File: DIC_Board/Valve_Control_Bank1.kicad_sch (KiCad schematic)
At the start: 10 parts, among them U20 DRV8823QDCARQ1

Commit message: Completed Acid Pump sheet
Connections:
- net GND: no longer C204.2
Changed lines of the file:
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@@
-		)
-	)
-	(label "GND"
-		(at 171.45 69.85 270)
-		(effects
-			(font
-				(size 1.27 1.27)
-			)
-			(justify right bottom)
 		)
 	)

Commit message: Wrapping up schematic
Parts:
- removed R200, R201, R202, R203: 3.3R, Resistor_SMD:R_1206_3216Metric, symbol Device:R_Small_US
- added R318, R319, R330, R331: 3.3R, Resistor_SMD:R_0402_1005Metric, symbol Device:R
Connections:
- net GND: now also C204.2, R318.2, R319.2, R330.2, R331.2
- net at U20.47 (BISEN): now also R319.1
- net at U20.21 (DISEN): now also R331.1
- net at U20.26 (CISEN): now also R330.1
- net at U20.4 (AISEN): now also R318.1
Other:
- moved on the sheet: C200, C201, C202, C203, C204, U20

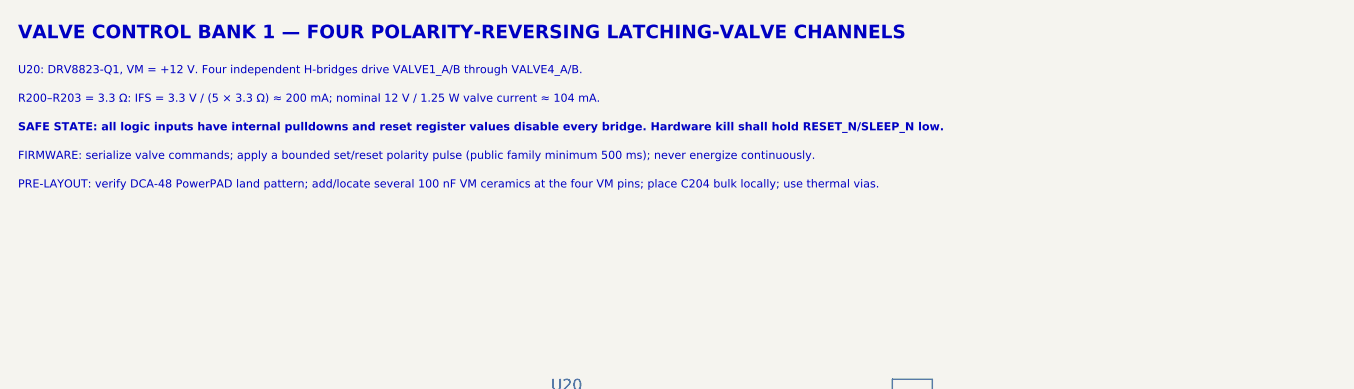
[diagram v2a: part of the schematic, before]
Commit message: Synchronize power, communications, and MCU configuration
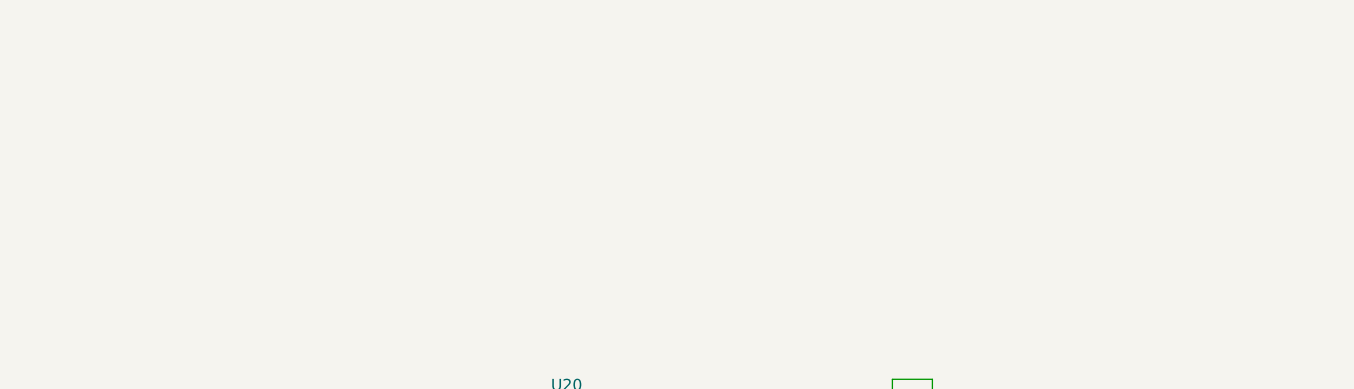
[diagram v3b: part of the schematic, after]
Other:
- note removed: "FIRMWARE: serialize valve commands; apply a bounded set/reset polarity pulse (public family minimum 500 ms); never energize continuously."
- note removed: "PRE-LAYOUT: verify DCA-48 PowerPAD land pattern; add/locate several 100 nF VM ceramics at the four VM pins; place C204 bulk locally; use thermal vias."
- note removed: "R200–R203 = 3.3 Ω: IFS = 3.3 V / (5 × 3.3 Ω) ≈ 200 mA; nominal 12 V / 1.25 W valve current ≈ 104 mA."
- note removed: "SAFE STATE: all logic inputs have internal pulldowns and reset register values disable every bridge. Hardware kill shall hold RESET_N/SLEEP_N low."
- note removed: "U20: DRV8823-Q1, VM = +12 V. Four independent H-bridges drive VALVE1_A/B through VALVE4_A/B."
- note removed: "VALVE CONTROL BANK 1 — FOUR POLARITY-REVERSING LATCHING-VALVE CHANNELS"
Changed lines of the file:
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@@
 		(comment 2 "DRV8823-Q1 serial quad H-bridge")
-	)
-	(text "U20: DRV8823-Q1, VM = +12 V. Four independent H-bridges drive VALVE1_A/B through VALVE4_A/B."
-		(exclude_from_sim no)
-		(at 25.4 24.13 0)
-		(effects
-			(font
-				(size 0.9 0.9)
-			)
-			(justify left bottom)
-		)
-	)
-	(text "FIRMWARE: serialize valve commands; apply a bounded set/reset polarity pulse (public family minimum 500 ms); never energize continuously."
-		(exclude_from_sim no)
-		(at 25.4 33.655 0)
-		(effects
-			(font
-				(size 0.9 0.9)
-			)
-			(justify left bottom)
-		)
-	)
-	(text "VALVE CONTROL BANK 1 — FOUR POLARITY-REVERSING LATCHING-VALVE CHANNELS"
-		(exclude_from_sim no)
-		(at 25.4 20.32 0)
-		(effects
-			(font
-				(size 1.5 1.5)
-				(bold yes)
-			)
-			(justify left bottom)
-		)
-	)
-	(text "R200–R203 = 3.3 Ω: IFS = 3.3 V / (5 × 3.3 Ω) ≈ 200 mA; nominal 12 V / 1.25 W valve current ≈ 104 mA."
-		(exclude_from_sim no)
-		(at 25.4 27.305 0)
-		(effects
-			(font
-				(size 0.9 0.9)
-			)
-			(justify left bottom)
-		)
-	)
-	(text "SAFE STATE: all logic inputs have internal pulldowns and reset register values disable every bridge. Hardware kill shall hold RESET_N/SLEEP_N low."
-		(exclude_from_sim no)
-		(at 25.4 30.48 0)
-		(effects
-			(font
-				(size 0.9 0.9)
-				(bold yes)
-			)
-			(justify left bottom)
-		)
-	)
-	(text "PRE-LAYOUT: verify DCA-48 PowerPAD land pattern; add/locate several 100 nF VM ceramics at the four VM pins; place C204 bulk locally; use thermal vias."
-		(exclude_from_sim no)
-		(at 25.4 36.83 0)
-		(effects
-			(font
-				(size 0.9 0.9)
-			)
-			(justify left bottom)
-		)
 	)
 	(junction

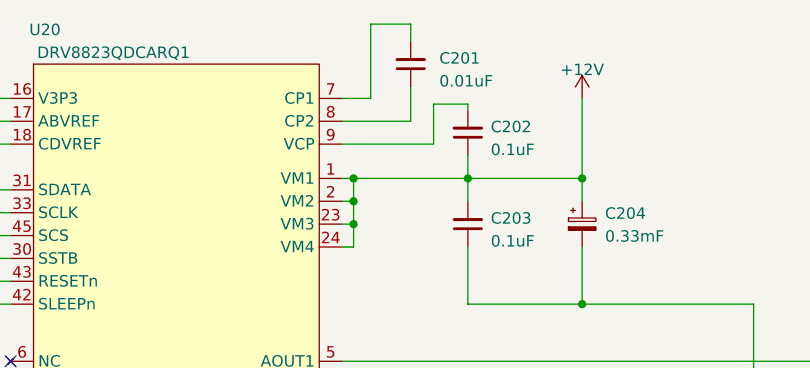
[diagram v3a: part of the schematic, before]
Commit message: Updated board for layout! All footprints added
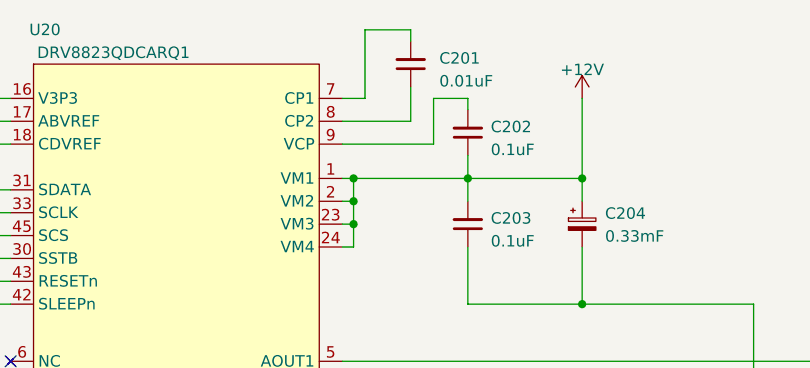
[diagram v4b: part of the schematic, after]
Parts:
- C200: Manufacturer (none) -> TDK
- C201, C202, C203: Manufacturer (none) -> KEMET
- C204: Manufacturer (none) -> Nichicon
- R318, R319, R330, R331: BOM Source (none) -> https://www.vishay.com/docs/20043/crcwhpe3.pdf; MPN (none) -> CRCW04023R30FKEDHP; Manufacturer Vishay Dale -> Vishay; Power Rating (none) -> 0.2W; Tolerance (none) -> 1%
- U20: footprint DIC_Board:HTSSOP48 -> DIC_Board:DRV8823_DCA48_ReviewFixed; Manufacturer (none) -> Texas Instruments
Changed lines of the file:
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@@
 	(wire
 		(pts
-			(xy 133.35 66.675) (xy 133.35 67.31)
+			(xy 133.35 66.04) (xy 133.35 67.31)
 		)
 		(stroke
@@
 	(wire
 		(pts
-			(xy 122.555 57.785) (xy 127 57.785)
+			(xy 121.92 58.42) (xy 127 58.42)
 		)
 		(stroke
@@
 	(wire
 		(pts
-			(xy 122.555 66.04) (xy 122.555 57.785)
+			(xy 121.92 66.04) (xy 121.92 58.42)
 		)
 		(stroke
@@
 	(wire
 		(pts
-			(xy 129.54 66.675) (xy 133.35 66.675)
-		)
-		(stroke
-			(width 0)
-			(type default)
-		)
-	)
-	(wire
-		(pts
-			(xy 129.54 71.12) (xy 129.54 66.675)
-		)
-		(stroke
-			(width 0)
-			(type default)
-		)
-	)
-	(wire
-		(pts
-			(xy 127 57.785) (xy 127 59.69)
+			(xy 129.54 66.04) (xy 133.35 66.04)
+		)
+		(stroke
+			(width 0)
+			(type default)
+		)
+	)
+	(wire
+		(pts
+			(xy 129.54 71.12) (xy 129.54 66.04)
+		)
+		(stroke
+			(width 0)
+			(type default)
+		)
+	)
+	(wire
+		(pts
+			(xy 127 58.42) (xy 127 59.69)
 		)
 		(stroke
@@
 	(wire
 		(pts
-			(xy 119.38 66.04) (xy 122.555 66.04)
+			(xy 119.38 66.04) (xy 121.92 66.04)
 		)
 		(stroke
@@
 			)
 		)
+		(property "Manufacturer" "TDK"
+			(at 0 0 0)
+			(hide yes)
+			(show_name no)
+			(do_not_autoplace no)
+			(effects
+				(font
+					(size 1.27 1.27)
+				)
+			)
+		)
 		(pin "1"
 		)
@@
 			)
 		)
+		(property "Manufacturer" "KEMET"
+			(at 0 0 0)
+			(hide yes)
+			(show_name no)
+			(do_not_autoplace no)
+			(effects
+				(font
+					(size 1.27 1.27)
+				)
+			)
+		)
 		(pin "1"
 		)
@@
 			)
 		)
-		(property "MPN" ""
+		(property "MPN" "CRCW04023R30FKEDHP"
 			(at 128.27 100.33 0)
 			(hide yes)
@@
 			)
 		)
-		(property "Manufacturer" "Vishay Dale"
+		(property "Manufacturer" "Vishay"
 			(at 128.27 100.33 0)
+			(hide yes)
+			(show_name no)
+			(do_not_autoplace no)
+			(effects
+				(font
+					(size 1.27 1.27)
+				)
+			)
+		)
+		(property "Tolerance" "1%"
+			(at 0 0 0)
+			(hide yes)
+			(show_name no)
+			(do_not_autoplace no)
+			(effects
+				(font
+					(size 1.27 1.27)
+				)
+			)
+		)
+		(property "Power Rating" "0.2W"
+			(at 0 0 0)
+			(hide yes)
+			(show_name no)
+			(do_not_autoplace no)
+			(effects
+				(font
+					(size 1.27 1.27)
+				)
+			)
+		)
+		(property "BOM Source" "https://www.vishay.com/docs/20043/crcwhpe3.pdf"
+			(at 0 0 0)
 			(hide yes)
 			(show_name no)
@@
 			)
 		)
-		(property "Footprint" "DIC_Board:HTSSOP48"
+		(property "Footprint" "DIC_Board:DRV8823_DCA48_ReviewFixed"
 			(at 90.17 69.85 0)
 			(hide yes)
@@
 		(property "MPN" "DRV8823QDCARQ1"
 			(at 85.09 62.23 0)
+			(hide yes)
+			(show_name no)
+			(do_not_autoplace no)
+			(effects
+				(font
+					(size 1.27 1.27)
+				)
+			)
+		)
+		(property "Manufacturer" "Texas Instruments"
+			(at 0 0 0)
 			(hide yes)
 			(show_name no)
@@
 			)
 		)
+		(property "Manufacturer" "KEMET"
+			(at 0 0 0)
+			(hide yes)
+			(show_name no)
+			(do_not_autoplace no)
+			(effects
+				(font
+					(size 1.27 1.27)
+				)
+			)
+		)
 		(pin "1"
 		)
@@
 			)
 		)
-		(property "MPN" ""
+		(property "MPN" "CRCW04023R30FKEDHP"
 			(at 128.27 146.05 0)
 			(hide yes)
@@
 			)
 		)
-		(property "Manufacturer" "Vishay Dale"
+		(property "Manufacturer" "Vishay"
 			(at 128.27 146.05 0)
+			(hide yes)
+			(show_name no)
+			(do_not_autoplace no)
+			(effects
+				(font
+					(size 1.27 1.27)
+				)
+			)
+		)
+		(property "Tolerance" "1%"
+			(at 0 0 0)
+			(hide yes)
+			(show_name no)
+			(do_not_autoplace no)
+			(effects
+				(font
+					(size 1.27 1.27)
+				)
+			)
+		)
+		(property "Power Rating" "0.2W"
+			(at 0 0 0)
+			(hide yes)
+			(show_name no)
+			(do_not_autoplace no)
+			(effects
+				(font
+					(size 1.27 1.27)
+				)
+			)
+		)
+		(property "BOM Source" "https://www.vishay.com/docs/20043/crcwhpe3.pdf"
+			(at 0 0 0)
 			(hide yes)
 			(show_name no)
@@
 			)
 		)
+		(property "Manufacturer" "KEMET"
+			(at 0 0 0)
+			(hide yes)
+			(show_name no)
+			(do_not_autoplace no)
+			(effects
+				(font
+					(size 1.27 1.27)
+				)
+			)
+		)
 		(pin "1"
 		)
@@
 			)
 		)
-		(property "MPN" ""
+		(property "MPN" "CRCW04023R30FKEDHP"
 			(at 128.27 130.81 0)
 			(hide yes)
@@
 			)
 		)
-		(property "Manufacturer" "Vishay Dale"
+		(property "Manufacturer" "Vishay"
 			(at 128.27 130.81 0)
+			(hide yes)
+			(show_name no)
+			(do_not_autoplace no)
+			(effects
+				(font
+					(size 1.27 1.27)
+				)
+			)
+		)
+		(property "Tolerance" "1%"
+			(at 0 0 0)
+			(hide yes)
+			(show_name no)
+			(do_not_autoplace no)
+			(effects
+				(font
+					(size 1.27 1.27)
+				)
+			)
+		)
+		(property "Power Rating" "0.2W"
+			(at 0 0 0)
+			(hide yes)
+			(show_name no)
+			(do_not_autoplace no)
+			(effects
+				(font
+					(size 1.27 1.27)
+				)
+			)
+		)
+		(property "BOM Source" "https://www.vishay.com/docs/20043/crcwhpe3.pdf"
+			(at 0 0 0)
 			(hide yes)
 			(show_name no)
@@
 			)
 		)
+		(property "Manufacturer" "Nichicon"
+			(at 0 0 0)
+			(hide yes)
+			(show_name no)
+			(do_not_autoplace no)
+			(effects
+				(font
+					(size 1.27 1.27)
+				)
+			)
+		)
 		(pin "1"
 		)
@@
 			)
 		)
-		(property "MPN" ""
+		(property "MPN" "CRCW04023R30FKEDHP"
 			(at 128.27 115.57 0)
 			(hide yes)
@@
 			)
 		)
-		(property "Manufacturer" "Vishay Dale"
+		(property "Manufacturer" "Vishay"
 			(at 128.27 115.57 0)
 			(hide yes)
 			(show_name no)
+			(do_not_autoplace no)
+			(effects
+				(font
+					(size 1.27 1.27)
+				)
+			)
+		)
+		(property "Tolerance" "1%"
+			(at 0 0 0)
+			(hide yes)
+			(show_name no)
+			(do_not_autoplace no)
+			(effects
+				(font
+					(size 1.27 1.27)
+				)
+			)
+		)
+		(property "Power Rating" "0.2W"
+			(at 0 0 0)
+			(hide yes)
+			(show_name no)
+			(do_not_autoplace no)
+			(effects
+				(font
+					(size 1.27 1.27)
+				)
+			)
+		)
+		(property "BOM Source" "https://www.vishay.com/docs/20043/crcwhpe3.pdf"
+			(at 0 0 0)
+			(hide yes)
+			(show_name no)

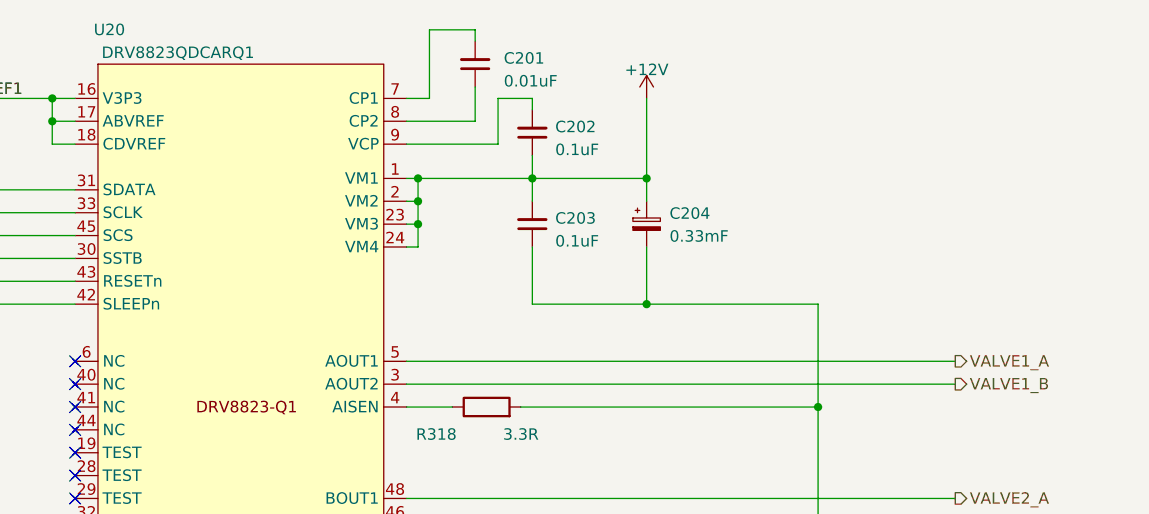
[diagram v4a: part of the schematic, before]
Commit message: Changed the 12V regulator to an integrated IC
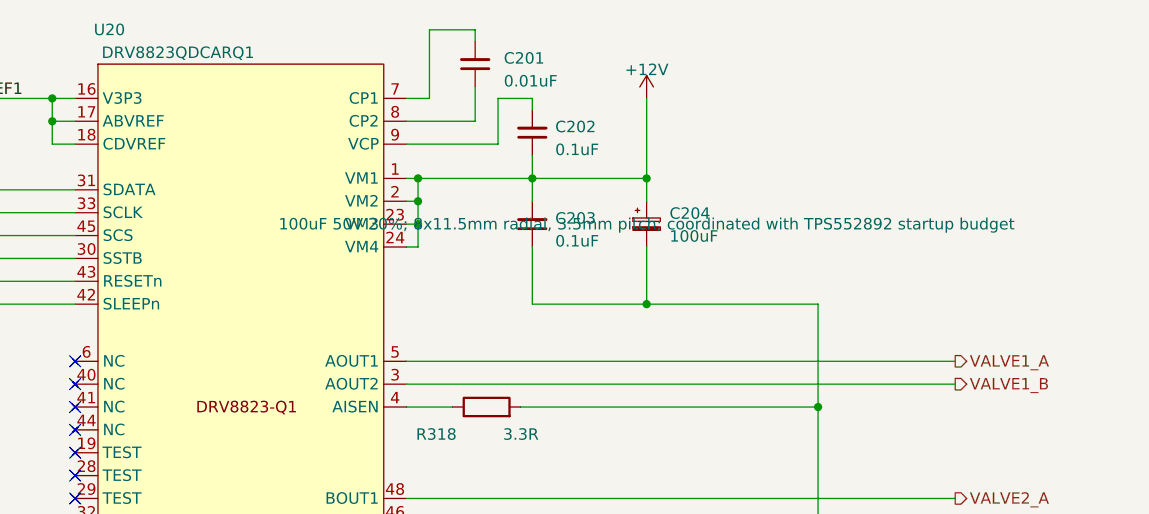
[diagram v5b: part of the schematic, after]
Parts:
- C204: value 0.33mF -> 100uF; footprint Capacitor_THT:CP_Radial_D12.5mm_P5.00mm -> Capacitor_THT:CP_Radial_D8.0mm_P3.50mm; MPN URZ1H331MHD1TO -> UHE1H101MPD
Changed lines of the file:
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@@
 			)
 		)
-		(property "Value" "0.33mF"
+		(property "Value" "100uF"
 			(at 148.59 81.3689 0)
 			(show_name no)
@@
 			)
 		)
-		(property "Footprint" "Capacitor_THT:CP_Radial_D12.5mm_P5.00mm"
+		(property "Footprint" "Capacitor_THT:CP_Radial_D8.0mm_P3.50mm"
 			(at 146.05 80.01 0)
 			(hide yes)
@@
 			)
 		)
-		(property "Datasheet" ""
+		(property "Datasheet" "https://www.nichicon.com/getmedia/5ee6e3a3-2d90-4858-bed0-89ef58a93bc3/e-uhe.pdf"
 			(at 146.05 80.01 0)
 			(hide yes)
@@
 			)
 		)
-		(property "Description" ""
+		(property "Description" "100uF 50V 20%; 8x11.5mm radial, 3.5mm pitch; coordinated with TPS552892 startup budget"
 			(at 146.05 80.01 0)
 			(show_name no)
@@
 			)
 		)
-		(property "MPN" "URZ1H331MHD1TO"
+		(property "MPN" "UHE1H101MPD"
 			(at 146.05 80.01 0)
 			(hide yes)
@@
 			(at 0 0 0)
 			(hide yes)
+			(show_name no)
+			(do_not_autoplace no)
+			(effects
+				(font
+					(size 1.27 1.27)
+				)
+			)
+		)
+		(property "Mouser" ""
+			(at 0 0 0)
+			(hide yes)
+			(show_name no)
+			(do_not_autoplace no)
+			(effects
+				(font
+					(size 1.27 1.27)
+				)
+			)
+		)
+		(property "DigiKey" ""
+			(at 0 0 0)
+			(hide yes)
